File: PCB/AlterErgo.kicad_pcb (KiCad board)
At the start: 2 copper layers, 105 parts, among them J1 GS3, J2 SJ-43514, J3 GS3, J4 Conn_01x02, SW0:10 SW_Push, SW0:11 SW_Push, SW0:12 SW_Push, SW0:7 SW_Push, SW0:8 SW_Push, SW0:9 SW_Push, SW1 SW_SPST, SW1:10 SW_Push, SW1:11 SW_Push, SW1:12 SW_Push, SW1:13 SW_Push, SW1:7 SW_Push, SW1:8 SW_Push, SW1:9 SW_Push, SW2:10 SW_Push, SW2:11 SW_Push, SW2:12 SW_Push, SW2:13 SW_Push, SW2:7 SW_Push, SW2:8 SW_Push, SW2:9 SW_Push, SW3:10 SW_Push, SW3:11 SW_Push, SW3:12 SW_Push, SW3:13 SW_Push, SW3:8 SW_Push, SW3:9 SW_Push, SW4:10 SW_Push, SW4:11 SW_Push, SW4:12 SW_Push, SW4:13 SW_Push, SW4:7 SW_Push, SW4:8 SW_Push, SW4:9 SW_Push, SW5:10 SW_Push, SW5:11 SW_Push, SW5:12 SW_Push, SW5:13 SW_Push, SW5:7 SW_Push, SW5:8 SW_Push, SW5:9 SW_Push, U1 Feather32u4Bluefruit, U2 MCP23018

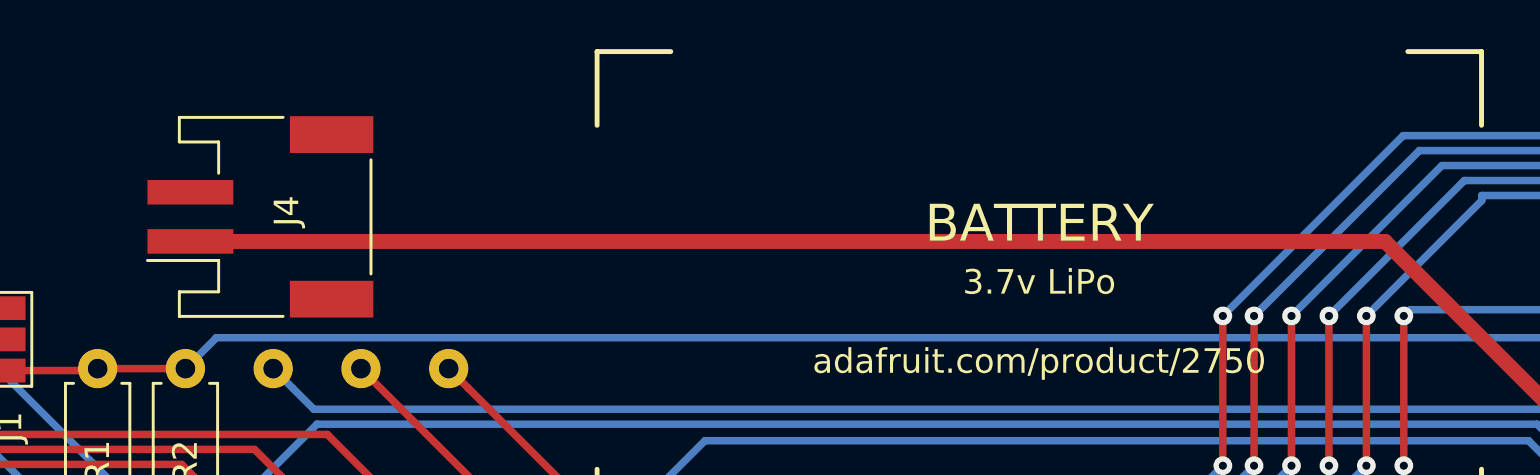
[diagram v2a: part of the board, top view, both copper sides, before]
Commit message: Allow mounting of battery connector on either side of PCB
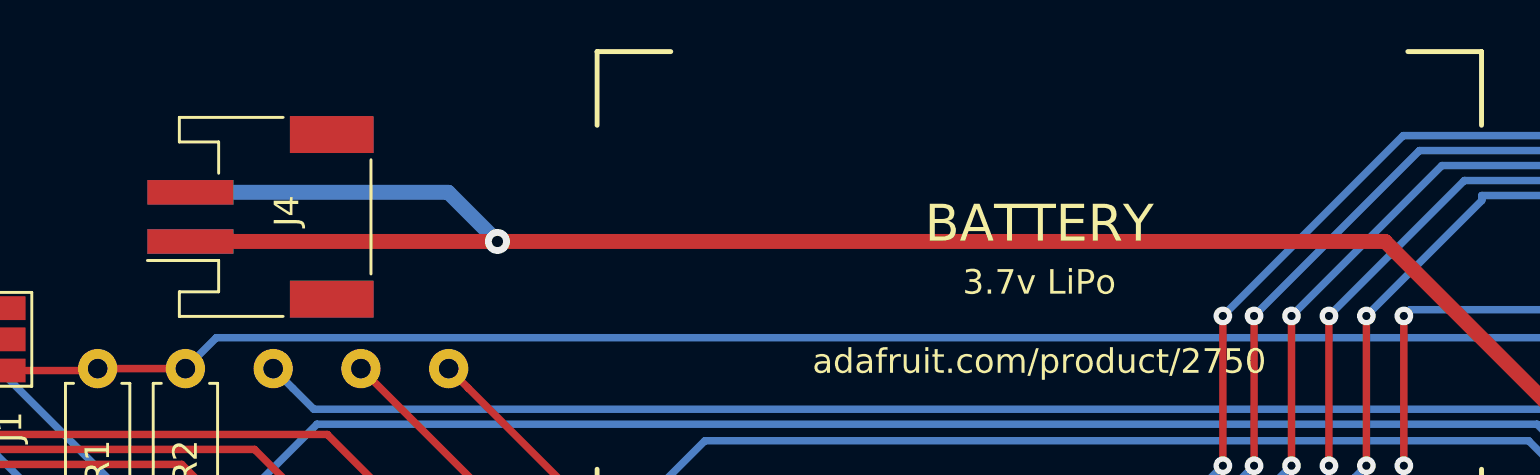
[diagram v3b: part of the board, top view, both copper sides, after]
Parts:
- added J4: Conn_01x02, Connectors_JST:JST_PH_S2B-PH-SM4-TB_02x2.00mm_Angled, B.Cu at (117.4, 28.4)
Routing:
- net Net-(J4-Pad1): track 109.5 -> 122.8 mm, vias 0 -> 1
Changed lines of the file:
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@@
 (kicad_pcb (version 4) (host pcbnew 4.0.7)
   (general
-    (links 0)
+    (links 546)
     (no_connects 15)
     (area 33.589001 -2.08962 221.067701 182.523514)
     (thickness 1.6)
     (drawings 68)
-    (tracks 1723)
+    (tracks 1727)
     (zones 0)
-    (modules 105)
+    (modules 106)
     (nets 69)
   )
@@
     (35 F.Paste user)
     (36 B.SilkS user)
-    (37 F.SilkS user)
+    (37 F.SilkS user hide)
     (38 B.Mask user)
     (39 F.Mask user)
@@
     (add_net "Net-(J4-Pad1)")
   )
+  (module Connectors_JST:JST_PH_S2B-PH-SM4-TB_02x2.00mm_Angled (layer B.Cu)
+    (at 117.378125 28.353125 270)
+    (descr "JST PH series connector, S2B-PH-SM4-TB, side entry type, surface mount, Datasheet: http://www.jst-mfg.com/product/pdf/eng/ePH.pdf")
+    (tags "connector jst ph")
+    (attr smd)
+    (fp_text reference J4 (at 0.240625 -1.053125 270) (layer B.SilkS)
+      (effects (font (size 1 1) (thickness 0.15)) (justify mirror))
+    )
+    (fp_text value Conn_01x02 (at 0 -5.375 270) (layer B.Fab)
+      (effects (font (size 1 1) (thickness 0.15)) (justify mirror))
+    )
+    (fp_line (start -3.15 1.625) (end -3.15 3.225) (layer B.Fab) (width 0.1))
+    (fp_line (start -3.15 3.225) (end -3.95 3.225) (layer B.Fab) (width 0.1))
+    (fp_line (start -3.95 3.225) (end -3.95 -4.375) (layer B.Fab) (width 0.1))
+    (fp_line (start -3.95 -4.375) (end 3.95 -4.375) (layer B.Fab) (width 0.1))
+    (fp_line (start 3.95 -4.375) (end 3.95 3.225) (layer B.Fab) (width 0.1))
+    (fp_line (start 3.95 3.225) (end 3.15 3.225) (layer B.Fab) (width 0.1))
+    (fp_line (start 3.15 3.225) (end 3.15 1.625) (layer B.Fab) (width 0.1))
+    (fp_line (start 3.15 1.625) (end -3.15 1.625) (layer B.Fab) (width 0.1))
+    (fp_line (start -1.775 1.725) (end -3.05 1.725) (layer B.SilkS) (width 0.12))
+    (fp_line (start -3.05 1.725) (end -3.05 3.325) (layer B.SilkS) (width 0.12))
+    (fp_line (start -3.05 3.325) (end -4.05 3.325) (layer B.SilkS) (width 0.12))
+    (fp_line (start -4.05 3.325) (end -4.05 -0.9) (layer B.SilkS) (width 0.12))
+    (fp_line (start 4.05 -0.9) (end 4.05 3.325) (layer B.SilkS) (width 0.12))
+    (fp_line (start 4.05 3.325) (end 3.05 3.325) (layer B.SilkS) (width 0.12))
+    (fp_line (start 3.05 3.325) (end 3.05 1.725) (layer B.SilkS) (width 0.12))
+    (fp_line (start 3.05 1.725) (end 1.775 1.725) (layer B.SilkS) (width 0.12))
+    (fp_line (start -2.325 -4.475) (end 2.325 -4.475) (layer B.SilkS) (width 0.12))
+    (fp_line (start -1.775 1.725) (end -1.775 4.625) (layer B.SilkS) (width 0.12))
+    (fp_line (start -2 1.625) (end -1 0.625) (layer B.Fab) (width 0.1))
+    (fp_line (start -1 0.625) (end 0 1.625) (layer B.Fab) (width 0.1))
+    (fp_line (start -4.6 5.13) (end -4.6 -5.07) (layer B.CrtYd) (width 0.05))
+    (fp_line (start -4.6 -5.07) (end 4.6 -5.07) (layer B.CrtYd) (width 0.05))
+    (fp_line (start 4.6 -5.07) (end 4.6 5.13) (layer B.CrtYd) (width 0.05))
+    (fp_line (start 4.6 5.13) (end -4.6 5.13) (layer B.CrtYd) (width 0.05))
+    (fp_text user %R (at 0 -3.434375 270) (layer B.Fab)
+      (effects (font (size 1 1) (thickness 0.15)) (justify mirror))
+    )
+    (pad 1 smd rect (at -1 2.875 270) (size 1 3.5) (layers B.Cu B.Paste B.Mask)
+      (net 68 "Net-(J4-Pad1)"))
+    (pad 2 smd rect (at 1 2.875 270) (size 1 3.5) (layers B.Cu B.Paste B.Mask)
+      (net 13 GND))
+    (pad "" smd rect (at -3.35 -2.875 270) (size 1.5 3.4) (layers B.Cu B.Paste B.Mask))
+    (pad "" smd rect (at 3.35 -2.875 270) (size 1.5 3.4) (layers B.Cu B.Paste B.Mask))
+    (model ${KISYS3DMOD}/Connectors_JST.3dshapes/JST_PH_S2B-PH-SM4-TB_02x2.00mm_Angled.wrl
+      (at (xyz 0 0 0))
+      (scale (xyz 1 1 1))
+      (rotate (xyz 0 0 0))
+    )
+  )
   (module keyswitches:MX_reversible_minimal (layer F.Cu)
     (at 200.025 140.49375 270)
@@
   (segment (start 169.9225 57.65895) (end 169.9225 59.21375) (width 0.3048) (layer F.Cu) (net 66))
   (segment (start 201.4855 42.545) (end 203.2635 44.323) (width 0.3048) (layer B.Cu) (net 66))
-  (segment (start 114.503125 29.353125) (end 163.1315 29.353125) (width 0.6096) (layer F.Cu) (net 68))
+  (segment (start 114.503125 29.353125) (end 127 29.353125) (width 0.6096) (layer F.Cu) (net 68))
+  (segment (start 127 29.353125) (end 163.1315 29.353125) (width 0.6096) (layer F.Cu) (net 68))
+  (segment (start 114.503125 27.353125) (end 125 27.353125) (width 0.6096) (layer B.Cu) (net 68))
+  (segment (start 125 27.353125) (end 127 29.353125) (width 0.6096) (layer B.Cu) (net 68))
+  (via (at 127 29.353125) (size 1.016) (drill 0.4572) (layers F.Cu B.Cu) (net 68) (status 1000000))
   (segment (start 163.1315 29.353125) (end 173.542154 39.763779) (width 0.6096) (layer F.Cu) (net 68))
   (segment (start 173.542154 39.763779) (end 207.826279 39.763779) (width 0.6096) (layer F.Cu) (net 68))

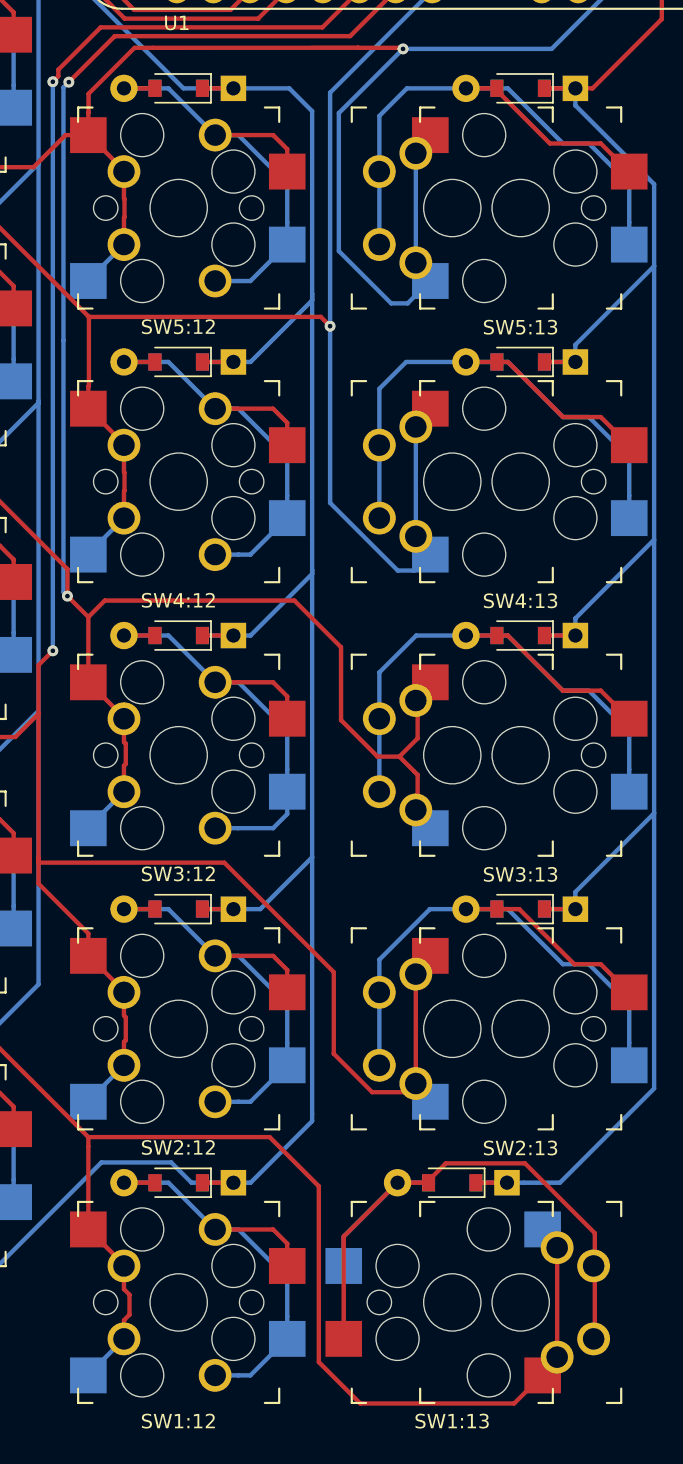
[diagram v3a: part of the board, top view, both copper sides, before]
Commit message: Fix footprints for alternate outer column positions so kicad recognizes the pins as needing to be connected
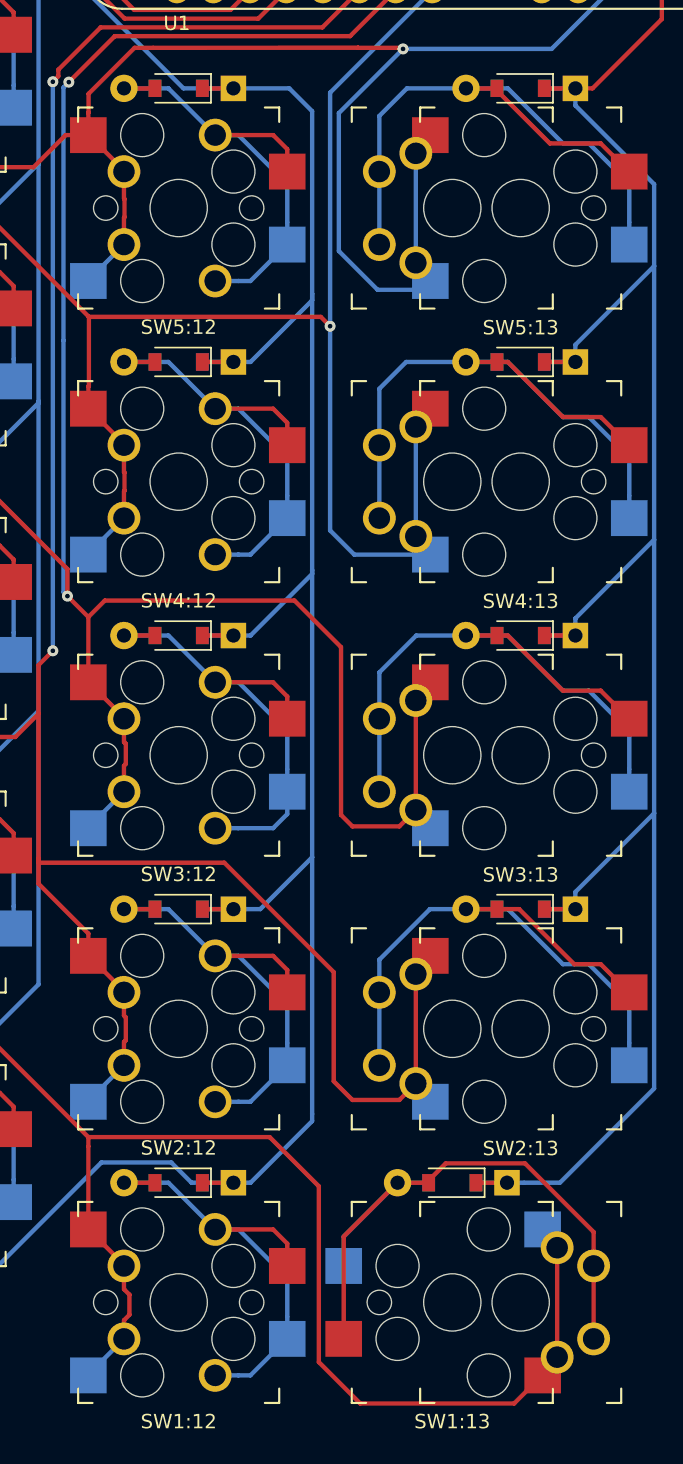
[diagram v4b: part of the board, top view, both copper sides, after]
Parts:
- removed ? (x5): MX, keyswitches:MX_reversible_minimal
- added SW1:13: SW_Push, keyswitches:MX_reversible_minimal, F.Cu at (200.0, 140.5)
- added SW2:13: SW_Push, keyswitches:MX_reversible_minimal, F.Cu at (195.3, 121.4)
- added SW3:13: SW_Push, keyswitches:MX_reversible_minimal, F.Cu at (195.3, 102.4)
- added SW4:13: SW_Push, keyswitches:MX_reversible_minimal, F.Cu at (195.3, 83.3)
- added SW5:13: SW_Push, keyswitches:MX_reversible_minimal, F.Cu at (195.3, 64.3)
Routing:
- net (no net): track 29.7 -> 0.00 mm
- net /ROW2: track 327.6 -> 341.1 mm
- net /ROW4: track 283.5 -> 294.9 mm
- net /ROW1: track 361.7 -> 372.7 mm
- net /ROW5: track 319.2 -> 329.3 mm
- net /ROW3: track 284.2 -> 292.3 mm

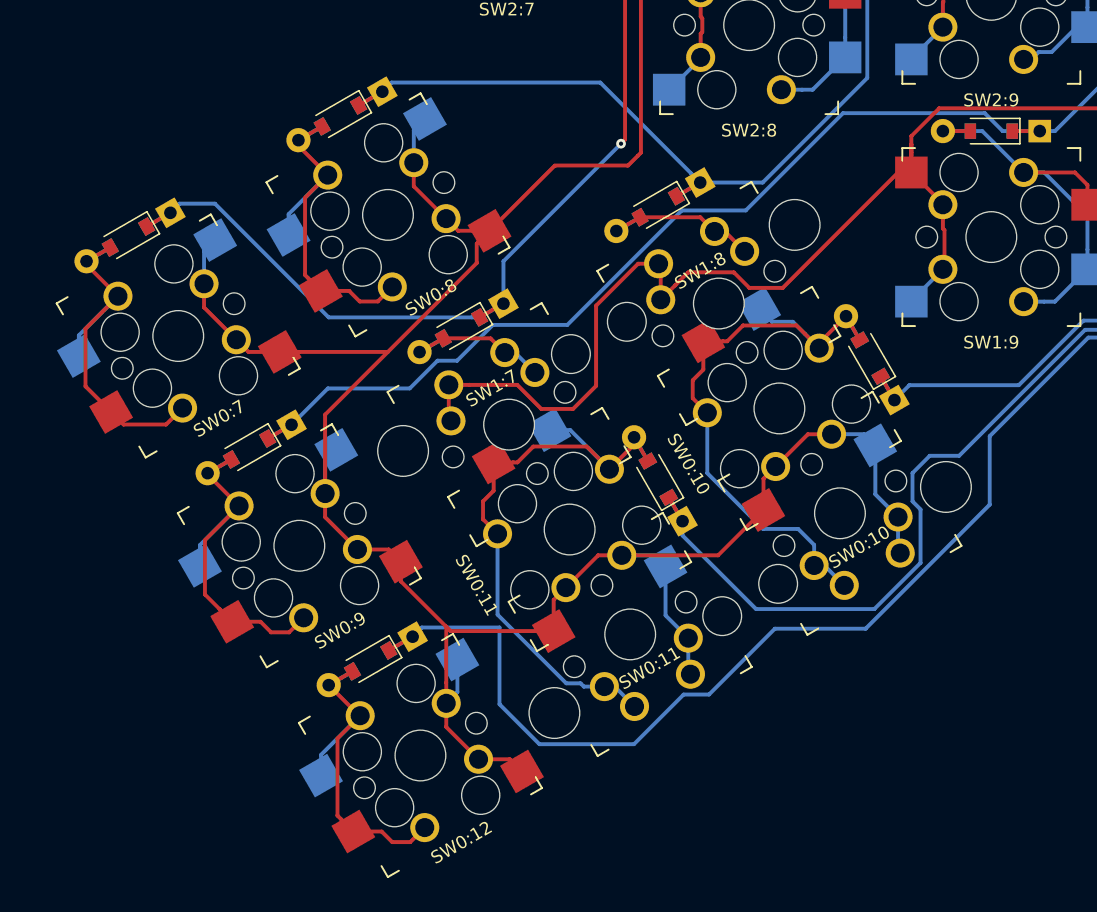
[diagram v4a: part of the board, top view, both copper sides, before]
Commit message: Move thumb cluster slightly
With key wobble, the innermost 2u thumb key and the closest key in the bottom row would have probably rubbed against each other, so moved the thumb cluster outward from the rest of the keyboard slightly
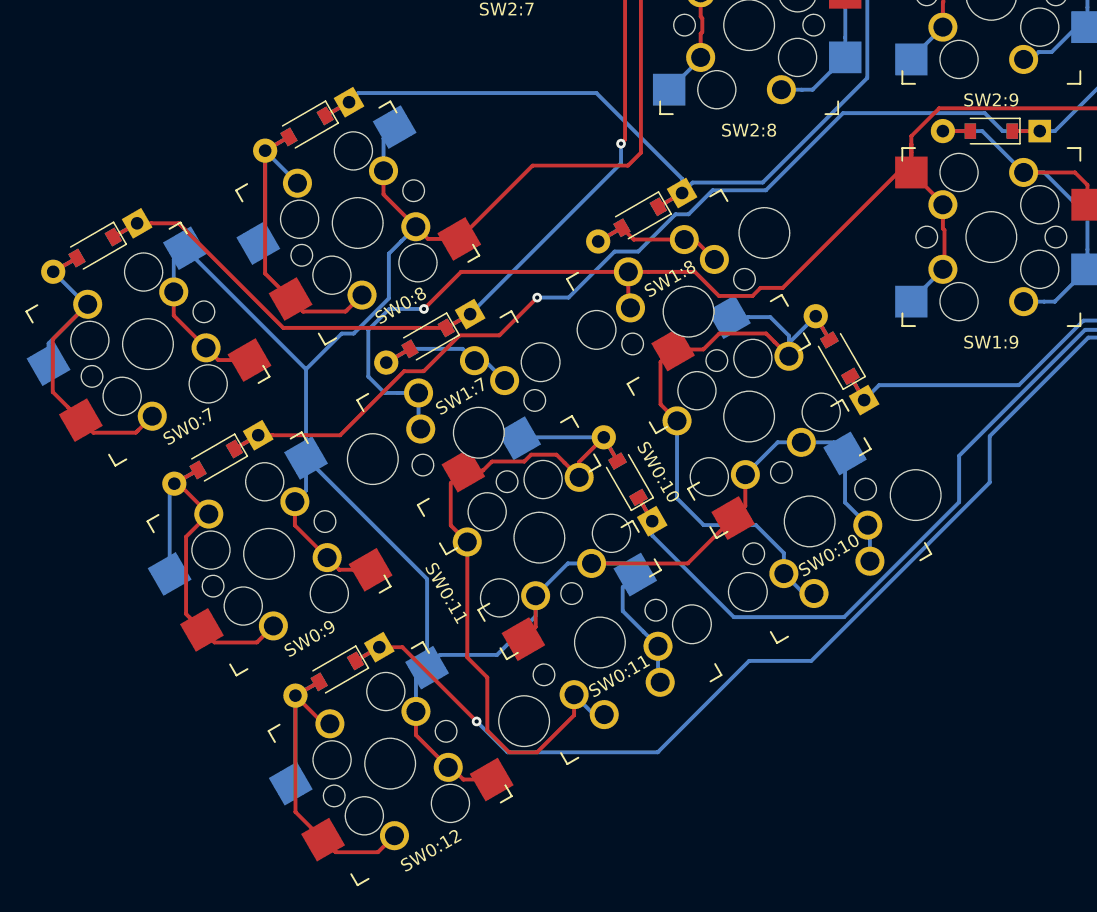
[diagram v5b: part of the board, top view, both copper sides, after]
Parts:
- moved D0:9 2.75 mm to (58.1, 148.5)
- moved D0:12 2.75 mm to (67.6, 165.1)
- moved D1:7 2.75 mm to (74.8, 138.9)
- moved D0:7 2.75 mm to (48.6, 131.8)
- moved D0:8 2.75 mm to (65.2, 122.3)
- moved SW0:8 2.47 mm to (69.2, 129.9)
- moved SW0:9 2.47 mm to (62.3, 155.9)
- moved SW0:11 2.47 mm to (88.3, 162.9)
- moved SW0:10 2.47 mm to (100.0, 145.1)
- moved SW0:10 2.47 mm to (104.8, 153.3)
- moved SW0:11 2.47 mm to (83.5, 154.6)
- moved SW0:7 2.47 mm to (52.7, 139.4)
- moved Stab0:10 2.47 mm to (100.0, 145.1)
- moved Stab0:11 2.47 mm to (83.5, 154.6)
- moved SW0:12 2.47 mm to (71.8, 172.4)
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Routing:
- net /ROW0: track 361.3 -> 377.1 mm
- net Net-(D0:11-Pad2): track 52.4 -> 60.7 mm
- net /ROW1: track 372.7 -> 379.7 mm, vias 2 -> 3
- net /COL5: track 285.8 -> 289.5 mm
- net /COL4: track 296.6 -> 299.5 mm, vias 2 -> 3
- net Net-(D0:8-Pad2): track 32.0 -> 34.5 mm
- net /COL10: track 260.4 -> 262.8 mm
- net /COL1: track 323.8 -> 321.4 mm, vias 2 -> 3
- net Net-(D0:10-Pad2): track 51.5 -> 53.2 mm
- net Net-(D0:7-Pad2): track 33.3 -> 31.8 mm
- net Net-(D0:12-Pad2): track 32.3 -> 33.8 mm
- net Net-(D1:8-Pad2): track 13.7 -> 12.6 mm
- net Net-(D0:9-Pad2): track 33.2 -> 32.2 mm
- net /COL6: track 297.8 -> 298.6 mm
